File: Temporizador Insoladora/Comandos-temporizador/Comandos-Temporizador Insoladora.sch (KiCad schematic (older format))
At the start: 5 parts, among them P7 CONN_02X08

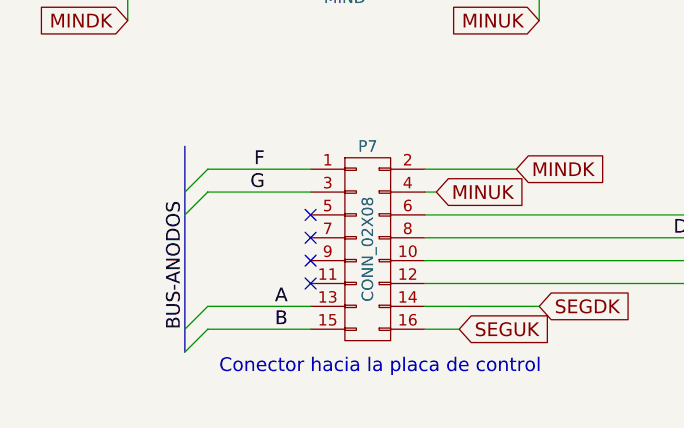
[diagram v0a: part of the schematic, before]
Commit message: Acomodando las referencias de los compònentes para el top silk
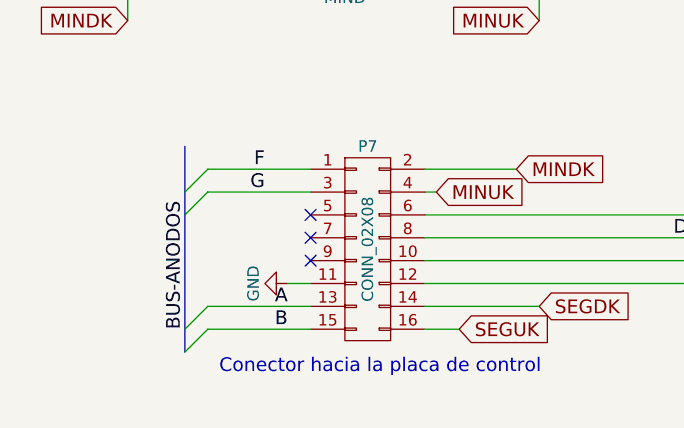
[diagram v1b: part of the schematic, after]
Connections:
- net GND: now also P7.11 (P11)
- no-connect marks 9 -> 8
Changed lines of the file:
@@
 NoConn ~ 3500 4000
 NoConn ~ 3500 4100
-NoConn ~ 3500 4200
+$Comp
+L GND #PWR03
+U 1 1 555F5789
+P 3400 4200
+F 0 "#PWR03" H 3400 3950 50  0001 C CNN
+F 1 "GND" H 3400 4050 50  0000 C CNN
+F 2 "" H 3400 4200 60  0000 C CNN
+F 3 "" H 3400 4200 60  0000 C CNN
+	1    3400 4200
+	0    1    1    0
+$EndComp
+Wire Wire Line
+	3400 4200 3500 4200
 $EndSCHEMATC
